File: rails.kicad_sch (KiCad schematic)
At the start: 94 parts, among them Q15 2N7002, U13 LM61460AASQRJRRQ1, U14 LM61460AASQRJRRQ1, U15 TPS259474ARPWR, U16 SN74LVC1G74, Y2 SX1M4.000M10F30TNN

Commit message: organize part fields
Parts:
- C122, C123, C124, C126, C127, C128, C141, C143, C177, C188, C189: Dielectric (none) -> X5R; MPN (none) -> TCC0603X5R106M350CT; Manufacturer (none) -> CCTC; Tolerance (none) -> 20%
- C125, C129, C135, C145: Dielectric (none) -> X5R; MPN (none) -> HGC0603R5225K500NTHJ; Manufacturer (none) -> Chinocera; Tolerance (none) -> 10%; Voltage Rating 16V -> 50V
- C131, C136: Capacitor Rating X7R -> (none); Dielectric (none) -> X7R; MPN (none) -> 0402B104J500NT; Manufacturer (none) -> FH (Fenghua); Tolerance (none) -> 5%
- C144, C147, C185: Dielectric (none) -> X5R; MPN (none) -> CL21A226MAYNNNE; Manufacturer (none) -> Samsung Electro-Mechanics; Tolerance (none) -> 20%; Voltage Rating 10V -> 25V
- C153, C158: Capacitor Rating C0G -> (none); Dielectric (none) -> C0G; MPN (none) -> FN15N5R6D500PNG; Manufacturer (none) -> PSA (Prosperity Dielectrics); Voltage Rating (none) -> 50V
- C155, C157, C165, C186: Dielectric (none) -> X5R; MPN (none) -> HGC0603R5226M160NTHJ; Manufacturer (none) -> Chinocera; Tolerance (none) -> 20%
- C156, C168, C169, C187, C190, C191, C192: Dielectric (none) -> X5R; MPN (none) -> TCC0603X5R106M350CT; Manufacturer (none) -> CCTC; Tolerance (none) -> 20%; Voltage Rating 16V -> 35V
- C159, C160: Dielectric (none) -> C0G; MPN (none) -> CC0402CG50V102JN; Manufacturer (none) -> TORCH; Tolerance (none) -> 5%; Voltage Rating 16V -> 50V
- C161, C162: Capacitor Rating C0G -> (none); Dielectric (none) -> C0G; MPN (none) -> GRM1555C1H222GA01D; Manufacturer (none) -> Murata; Tolerance (none) -> 2%; Voltage Rating (none) -> 50V
- C163, C164: Dielectric (none) -> X7R; MPN (none) -> TCC0402X7R105K250AT; Manufacturer (none) -> CCTC; Tolerance (none) -> 10%; Voltage Rating 16V -> 25V
- D20: MPN (none) -> SMF6.0A; Manufacturer (none) -> UMW
- D21: MPN (none) -> BAT54A; Manufacturer (none) -> ALJ
- D22: MPN (none) -> BAT54W; Manufacturer (none) -> Slkor
- L4: MPN (none) -> CMLO1040H2R2MTT; Manufacturer (none) -> Cybermax; Tolerance (none) -> 20%
- L5: MPN (none) -> CMLO1040H3R3MTT; Manufacturer (none) -> Cybermax; Tolerance (none) -> 20%
- Q15: MPN (none) -> 2N7002; Manufacturer (none) -> MSKSEMI
- R103, R111, R117: MPN (none) -> FRH0402D1000TS; Manufacturer (none) -> FOJAN; Power Rating (none) -> 62.5mW; Tolerance (none) -> 0.5%
- R104, R107: MPN (none) -> TC0350B4023T5F; Manufacturer (none) -> UNI-ROYAL; Power Rating (none) -> 100mW; Tolerance (none) -> 0.1%
- R105, R106, R108, R130, R131: MPN (none) -> ARG02BTC1003; Manufacturer (none) -> Viking Tech; Power Rating (none) -> 62.5mW; Tolerance (none) -> 0.1%
- R109, R110: MPN (none) -> RT0402BRD076K04L; Manufacturer (none) -> YAGEO; Power Rating (none) -> 62.5mW; Tolerance 1% -> 0.1%
- R112, R118: LCSC Part C5925229 -> C2078808; MPN (none) -> CRCW08052R20FKEAHP; Manufacturer (none) -> Vishay; Power Rating 250mW -> 500mW; Tolerance (none) -> 1%
- R113, R119, R132: MPN (none) -> FRH0402D1002TS; Manufacturer (none) -> FOJAN; Power Rating (none) -> 62.5mW; Tolerance (none) -> 0.5%
- R114, R120: MPN (none) -> 1RC0402F1009; Manufacturer (none) -> SAE; Power Rating (none) -> 62.5mW; Tolerance (none) -> 1%
- R115, R121: MPN (none) -> TC0350B4023T5F; Manufacturer (none) -> UNI-ROYAL; Power Rating (none) -> 100mW
- R116: MPN (none) -> RT0402BRD07174KL; Manufacturer (none) -> YAGEO; Power Rating (none) -> 62.5mW
- R122: MPN (none) -> RT0805BRD07101KL; Manufacturer (none) -> YAGEO; Power Rating (none) -> 125mW
- R123, R124: MPN (none) -> FRH0402B1001TS; Manufacturer (none) -> FOJAN; Power Rating (none) -> 62.5mW; Tolerance (none) -> 0.1%
- R125: MPN (none) -> RT0402BRD0786K6L; Manufacturer (none) -> YAGEO; Power Rating (none) -> 62.5mW
- R126: MPN (none) -> PTFR0402B3K92P9; Manufacturer (none) -> RESI; Power Rating (none) -> 60mW
- R127: MPN (none) -> RT0402BRD0727K4L; Manufacturer (none) -> YAGEO; Power Rating (none) -> 62.5mW
- R128: LCSC Part (none) -> C172092; MPN (none) -> WR04X5490FTL; Manufacturer (none) -> Walsin; Power Rating (none) -> 62.5mW
- R129: MPN (none) -> RT0603BRD07280KL; Manufacturer (none) -> YAGEO; Power Rating (none) -> 100mW; Tolerance (none) -> 0.1%
- U13, U14, U15: Manufacturer TI(德州仪器) -> Texas Instruments
- U16: MPN (none) -> SN74LVC1G74DQER; Manufacturer (none) -> Texas Instruments
- Y2: MPN (none) -> SX1M4.000M10F30TNN; Manufacturer (none) -> SCTF

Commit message: add extra PWR_FLAGs
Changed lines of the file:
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@@
 	)
 	(junction
-		(at 179.07 60.96)
-		(diameter 0)
-		(color 0 0 0 0)
-	)
-	(junction
 		(at 172.72 66.04)
 		(diameter 0)
@@
 	(wire
 		(pts
+			(xy 234.95 48.26) (xy 234.95 49.53)
+		)
+		(stroke
+			(width 0)
+			(type default)
+		)
+	)
+	(wire
+		(pts
 			(xy 80.01 63.5) (xy 80.01 64.77)
 		)
@@
 	(wire
 		(pts
-			(xy 179.07 57.15) (xy 179.07 60.96)
-		)
-		(stroke
-			(width 0)
-			(type default)
-		)
-	)
-	(wire
-		(pts
 			(xy 52.07 148.59) (xy 52.07 149.86)
 		)
@@
 	(wire
 		(pts
+			(xy 241.3 49.53) (xy 234.95 49.53)
+		)
+		(stroke
+			(width 0)
+			(type default)
+		)
+	)
+	(wire
+		(pts
 			(xy 52.07 140.97) (xy 52.07 148.59)
 		)
@@
 	(wire
 		(pts
-			(xy 179.07 60.96) (xy 172.72 60.96)
+			(xy 172.72 60.96) (xy 181.61 60.96)
 		)
 		(stroke
@@
 	(wire
 		(pts
-			(xy 181.61 60.96) (xy 179.07 60.96)
-		)
-		(stroke
-			(width 0)
-			(type default)
-		)
-	)
-	(wire
-		(pts
 			(xy 190.5 91.44) (xy 190.5 92.71)
 		)
@@
 	(wire
 		(pts
-			(xy 234.95 45.72) (xy 234.95 49.53)
+			(xy 241.3 45.72) (xy 241.3 49.53)
 		)
 		(stroke
@@
 	)
 	(symbol
-		(lib_id "power:PWR_FLAG")
-		(at 179.07 57.15 0)
-		(unit 1)
-		(body_style 1)
-		(exclude_from_sim no)
-		(in_bom yes)
-		(on_board yes)
-		(in_pos_files yes)
-		(dnp no)
-		(fields_autoplaced yes)
-		(property "Reference" "#FLG07"
-			(at 179.07 55.245 0)
-			(hide yes)
-			(show_name no)
-			(do_not_autoplace no)
-			(effects
-				(font
-					(size 1.27 1.27)
-				)
-			)
-		)
-		(property "Value" "PWR_FLAG"
-			(at 179.07 52.07 0)
-			(show_name no)
-			(do_not_autoplace no)
-			(effects
-				(font
-					(size 1.27 1.27)
-				)
-			)
-		)
-		(property "Footprint" ""
-			(at 179.07 57.15 0)
-			(hide yes)
-			(show_name no)
-			(do_not_autoplace no)
-			(effects
-				(font
-					(size 1.27 1.27)
-				)
-			)
-		)
-		(property "Datasheet" ""
-			(at 179.07 57.15 0)
-			(hide yes)
-			(show_name no)
-			(do_not_autoplace no)
-			(effects
-				(font
-					(size 1.27 1.27)
-				)
-			)
-		)
-		(property "Description" "Special symbol for telling ERC where power comes from"
-			(at 179.07 57.15 0)
-			(hide yes)
-			(show_name no)
-			(do_not_autoplace no)
-			(effects
-				(font
-					(size 1.27 1.27)
-				)
-			)
-		)
-		(pin "1"
-		)
-		(instances
-			(project "parsnip"
-				(path "/fe9d4a31-2311-442f-997c-52ad8ca5cfe9/ef3187a0-acf7-454f-a4ee-a309d9d8c27d"
-					(reference "#FLG07")
-					(unit 1)
-				)
-			)
-		)
-	)
-	(symbol
 		(lib_id "Connector:TestPoint_2Pole")
 		(at 190.5 149.86 90)
@@
 	)
 	(symbol
+		(lib_id "power:PWR_FLAG")
+		(at 234.95 48.26 0)
+		(unit 1)
+		(body_style 1)
+		(exclude_from_sim no)
+		(in_bom yes)
+		(on_board yes)
+		(in_pos_files yes)
+		(dnp no)
+		(property "Reference" "#FLG07"
+			(at 234.95 46.355 0)
+			(hide yes)
+			(show_name no)
+			(do_not_autoplace no)
+			(effects
+				(font
+					(size 1.27 1.27)
+				)
+			)
+		)
+		(property "Value" "PWR_FLAG"
+			(at 234.95 44.196 0)
+			(show_name no)
+			(do_not_autoplace no)
+			(effects
+				(font
+					(size 1.27 1.27)
+				)
+			)
+		)
+		(property "Footprint" ""
+			(at 234.95 48.26 0)
+			(hide yes)
+			(show_name no)
+			(do_not_autoplace no)
+			(effects
+				(font
+					(size 1.27 1.27)
+				)
+			)
+		)
+		(property "Datasheet" ""
+			(at 234.95 48.26 0)
+			(hide yes)
+			(show_name no)
+			(do_not_autoplace no)
+			(effects
+				(font
+					(size 1.27 1.27)
+				)
+			)
+		)
+		(property "Description" "Special symbol for telling ERC where power comes from"
+			(at 234.95 48.26 0)
+			(hide yes)
+			(show_name no)
+			(do_not_autoplace no)
+			(effects
+				(font
+					(size 1.27 1.27)
+				)
+			)
+		)
+		(pin "1"
+		)
+		(instances
+			(project "parsnip"
+				(path "/fe9d4a31-2311-442f-997c-52ad8ca5cfe9/ef3187a0-acf7-454f-a4ee-a309d9d8c27d"
+					(reference "#FLG07")
+					(unit 1)
+				)
+			)
+		)
+	)
+	(symbol
 		(lib_id "Device:C_Small")
 		(at 154.94 80.01 0)
@@
 	(symbol
 		(lib_id "power:+5V")
-		(at 234.95 45.72 0)
+		(at 241.3 45.72 0)
 		(unit 1)
 		(body_style 1)
@@
 		(fields_autoplaced yes)
 		(property "Reference" "#PWR0161"
-			(at 234.95 49.53 0)
+			(at 241.3 49.53 0)
 			(hide yes)
 			(show_name no)
@@
 		)
 		(property "Value" "+5V"
-			(at 234.95 40.64 0)
+			(at 241.3 40.64 0)
 			(show_name no)
 			(do_not_autoplace no)
@@
 		)
 		(property "Footprint" ""
-			(at 234.95 45.72 0)
+			(at 241.3 45.72 0)
 			(hide yes)
 			(show_name no)
@@
 		)
 		(property "Datasheet" ""
-			(at 234.95 45.72 0)
+			(at 241.3 45.72 0)
 			(hide yes)
 			(show_name no)
@@
 		)
 		(property "Description" "Power symbol creates a global label with name \"+5V\""
-			(at 234.95 45.72 0)
+			(at 241.3 45.72 0)
 			(hide yes)
 			(show_name no)

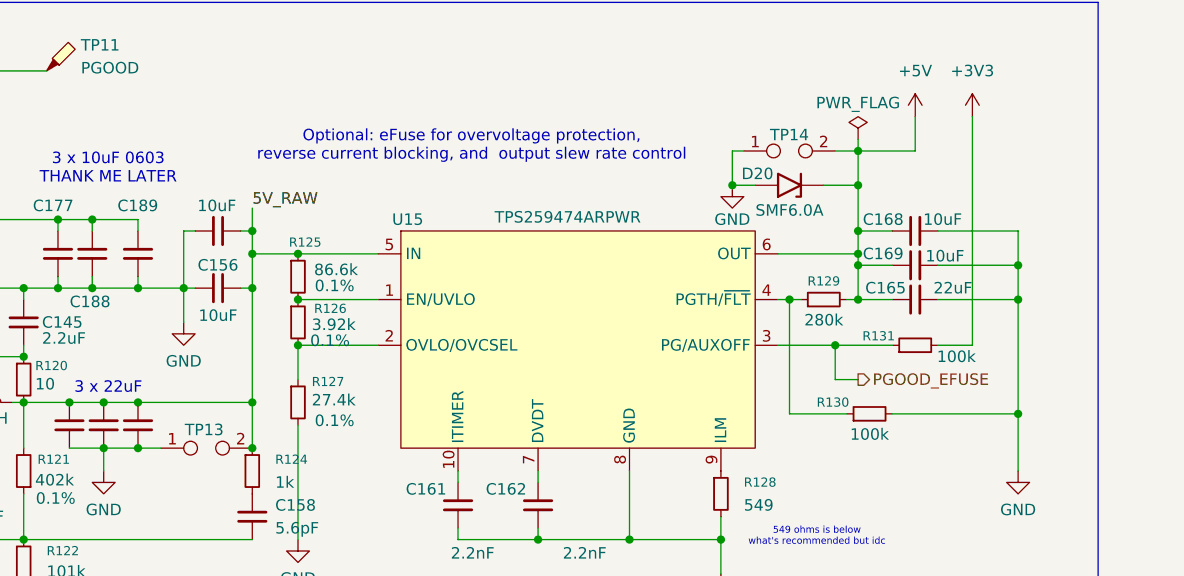
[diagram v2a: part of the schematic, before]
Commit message: routing and silkscreen improvements
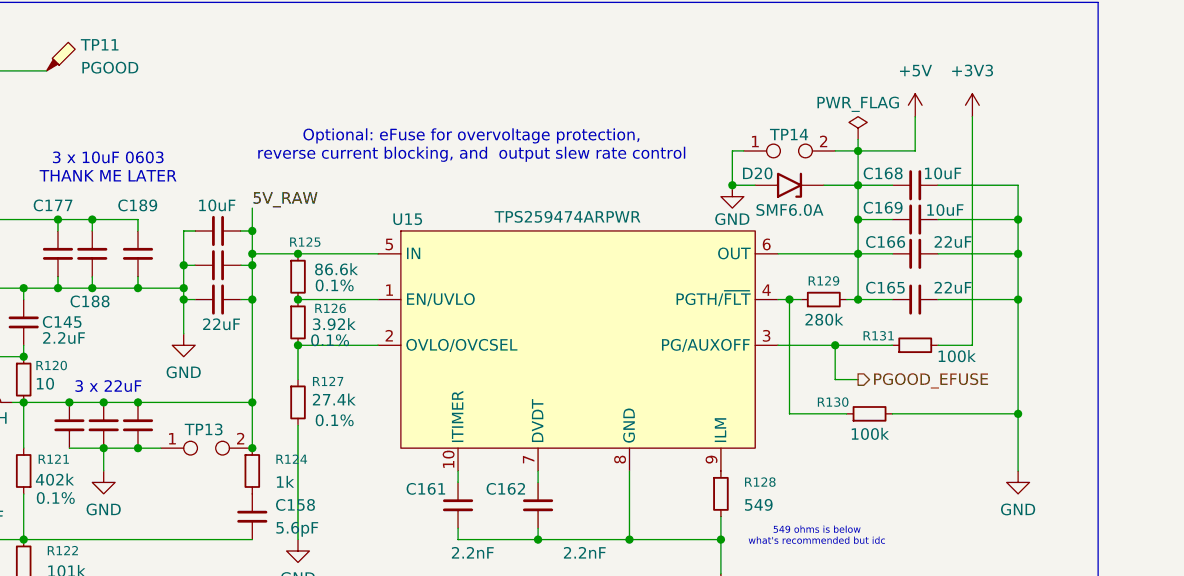
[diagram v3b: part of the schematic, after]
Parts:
- added C166, C167: 22uF, Capacitor_SMD:C_0603_1608Metric, symbol Device:C_Small
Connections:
- net +5V: now also C166.1
- net 5V_RAW: now also C167.2
- net GND: now also C166.2, C167.1
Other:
- moved on the sheet: C168, C169

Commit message: nearly set to order!
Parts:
- L4: footprint Inductor_SMD:L_Sunlord_MWSA1003S -> Inductor_SMD:L_APV_APH1040
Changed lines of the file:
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@@
 			)
 		)
-		(property "Footprint" "Inductor_SMD:L_Sunlord_MWSA1003S"
+		(property "Footprint" "Inductor_SMD:L_APV_APH1040"
 			(at 121.92 161.29 0)
 			(hide yes)
@@
 			(at 121.92 161.29 0)
 			(hide yes)
+			(show_name no)
+			(do_not_autoplace no)
+			(effects
+				(font
+					(size 1.27 1.27)
+				)
+			)
+		)
+		(property "Voltage Rating" ""
+			(at 121.92 161.29 0)
+			(hide yes)
